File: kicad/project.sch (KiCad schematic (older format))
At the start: 23 parts, among them J1 SWD, U1 STM32L031F4Px

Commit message: Libraries
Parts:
- J1: symbol CONN_01X05 -> Conn_01x05
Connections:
- wire segments 12 -> 9
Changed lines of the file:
@@
 EESchema Schematic File Version 2
+LIBS:project-rescue
 LIBS:power
 LIBS:device
@@
 LIBS:valves
 LIBS:stm32_theapi
-LIBS:project-cache
 EELAYER 25 0
 EELAYER END
@@
 $EndComp
 $Comp
-L CONN_01X05 J1
+L Conn_01x05 J1
 U 1 1 5A9FF0BA
 P 2825 3625
@@
 	3025 3625 3525 3625
 Wire Wire Line
-	5575 2325 5575 2525
-Wire Wire Line
-	5575 2525 5575 2925
-Wire Wire Line
-	5675 2325 5675 2525
-Wire Wire Line
-	5675 2525 5675 2925
-Wire Wire Line
-	5575 2325 5625 2325
-Wire Wire Line
-	5625 2325 5675 2325
+	5575 2325 5575 2925
+Wire Wire Line
+	5675 2325 5675 2925
+Wire Wire Line
+	5575 2325 5675 2325
 Connection ~ 5625 2325
 Connection ~ 5675 2525

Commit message: Initial led placement
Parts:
- BT1: footprint Pin_Headers:Pin_Header_Straight_2x01_Pitch2.54mm -> theapi:CR2032H
- D1, D2, D3, D4, D5, D6, D7, D8: footprint (none) -> LEDs:LED_0805
- R2, R3, R4, R5, R6, R7, R8, R9: footprint (none) -> Resistors_SMD:R_0603_HandSoldering
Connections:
- net at U1.10 (PA4): now also R6.2
- net at U1.11 (PA5): now also R7.2
- net at U1.12 (PA6): now also R8.2
- net at U1.13 (PA7): now also R9.2
- net at U1.6 (PA0): now also R2.2
- net at U1.7 (PA1): now also R3.2
- net at U1.8 (PA2): now also R4.2
- net at U1.9 (PA3): now also R5.2
- no-connect marks 0 -> 5
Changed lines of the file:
@@
 LIBS:valves
 LIBS:stm32_theapi
+LIBS:project-cache
 EELAYER 25 0
 EELAYER END
@@
 $EndComp
 $Comp
-L GND #PWR13
+L GND #PWR01
 U 1 1 5A9FF0BC
 P 4950 3925
-F 0 "#PWR13" H 4950 3675 50  0001 C CNN
+F 0 "#PWR01" H 4950 3675 50  0001 C CNN
 F 1 "GND" H 4950 3775 50  0000 C CNN
 F 2 "" H 4950 3925 50  0001 C CNN
@@
 $EndComp
 $Comp
-L GND #PWR16
+L GND #PWR02
 U 1 1 5A9FF0BD
 P 5675 4825
-F 0 "#PWR16" H 5675 4575 50  0001 C CNN
+F 0 "#PWR02" H 5675 4575 50  0001 C CNN
 F 1 "GND" H 5675 4675 50  0000 C CNN
 F 2 "" H 5675 4825 50  0001 C CNN
@@
 SWDIO
 $Comp
-L +BATT #PWR4
+L +BATT #PWR03
 U 1 1 5A9FF0BE
 P 5625 2325
-F 0 "#PWR4" H 5625 2175 50  0001 C CNN
+F 0 "#PWR03" H 5625 2175 50  0001 C CNN
 F 1 "+BATT" H 5625 2465 50  0000 C CNN
 F 2 "" H 5625 2325 50  0001 C CNN
@@
 $EndComp
 $Comp
-L +BATT #PWR10
+L +BATT #PWR04
 U 1 1 5A9FF0BF
 P 3025 3425
-F 0 "#PWR10" H 3025 3275 50  0001 C CNN
+F 0 "#PWR04" H 3025 3275 50  0001 C CNN
 F 1 "+BATT" H 3025 3565 50  0000 C CNN
 F 2 "" H 3025 3425 50  0001 C CNN
@@
 $EndComp
 $Comp
-L GND #PWR11
+L GND #PWR05
 U 1 1 5A9FF0C0
 P 3525 3625
-F 0 "#PWR11" H 3525 3375 50  0001 C CNN
+F 0 "#PWR05" H 3525 3375 50  0001 C CNN
 F 1 "GND" H 3525 3475 50  0000 C CNN
 F 2 "" H 3525 3625 50  0001 C CNN
@@
 F 0 "BT1" H 4150 1675 50  0000 L CNN
 F 1 "Battery_Cell" H 4150 1575 50  0000 L CNN
-F 2 "Pin_Headers:Pin_Header_Straight_2x01_Pitch2.54mm" V 4050 1635 50  0001 C CNN
+F 2 "theapi:CR2032H" V 4050 1635 50  0001 C CNN
 F 3 "" V 4050 1635 50  0001 C CNN
 	1    4050 1575
@@
 $EndComp
 $Comp
-L +BATT #PWR1
+L +BATT #PWR06
 U 1 1 5A9FF0C2
 P 4050 1375
-F 0 "#PWR1" H 4050 1225 50  0001 C CNN
+F 0 "#PWR06" H 4050 1225 50  0001 C CNN
 F 1 "+BATT" H 4050 1515 50  0000 C CNN
 F 2 "" H 4050 1375 50  0001 C CNN
@@
 $EndComp
 $Comp
-L GND #PWR2
+L GND #PWR07
 U 1 1 5A9FF0C3
 P 4050 1675
-F 0 "#PWR2" H 4050 1425 50  0001 C CNN
+F 0 "#PWR07" H 4050 1425 50  0001 C CNN
 F 1 "GND" H 4050 1525 50  0000 C CNN
 F 2 "" H 4050 1675 50  0001 C CNN
@@
 $EndComp
 $Comp
-L GND #PWR5
+L GND #PWR08
 U 1 1 5A9FF0C6
 P 5375 2525
-F 0 "#PWR5" H 5375 2275 50  0001 C CNN
+F 0 "#PWR08" H 5375 2275 50  0001 C CNN
 F 1 "GND" H 5375 2375 50  0000 C CNN
 F 2 "" H 5375 2525 50  0001 C CNN
@@
 $EndComp
 $Comp
-L GND #PWR6
+L GND #PWR09
 U 1 1 5A9FF0C7
 P 5875 2525
-F 0 "#PWR6" H 5875 2275 50  0001 C CNN
+F 0 "#PWR09" H 5875 2275 50  0001 C CNN
 F 1 "GND" H 5875 2375 50  0000 C CNN
 F 2 "" H 5875 2525 50  0001 C CNN
@@
 F 0 "D1" H 9025 2275 50  0000 C CNN
 F 1 "LED" H 9025 2075 50  0000 C CNN
-F 2 "" H 9025 2175 50  0001 C CNN
+F 2 "LEDs:LED_0805" H 9025 2175 50  0001 C CNN
 F 3 "" H 9025 2175 50  0001 C CNN
 	1    9025 2175
@@
 $EndComp
 $Comp
-L GND #PWR3
+L GND #PWR010
 U 1 1 5A9FF286
 P 9175 2175
-F 0 "#PWR3" H 9175 1925 50  0001 C CNN
+F 0 "#PWR010" H 9175 1925 50  0001 C CNN
 F 1 "GND" H 9175 2025 50  0000 C CNN
 F 2 "" H 9175 2175 50  0001 C CNN
@@
 F 0 "R2" V 8805 2175 50  0000 C CNN
 F 1 "1k" V 8725 2175 50  0000 C CNN
-F 2 "" V 8655 2175 50  0001 C CNN
+F 2 "Resistors_SMD:R_0603_HandSoldering" V 8655 2175 50  0001 C CNN
 F 3 "" H 8725 2175 50  0001 C CNN
 	1    8725 2175
@@
 F 0 "D2" H 9025 2650 50  0000 C CNN
 F 1 "LED" H 9025 2450 50  0000 C CNN
-F 2 "" H 9025 2550 50  0001 C CNN
+F 2 "LEDs:LED_0805" H 9025 2550 50  0001 C CNN
 F 3 "" H 9025 2550 50  0001 C CNN
 	1    9025 2550
@@
 $EndComp
 $Comp
-L GND #PWR7
+L GND #PWR011
 U 1 1 5A9FF752
 P 9175 2550
-F 0 "#PWR7" H 9175 2300 50  0001 C CNN
+F 0 "#PWR011" H 9175 2300 50  0001 C CNN
 F 1 "GND" H 9175 2400 50  0000 C CNN
 F 2 "" H 9175 2550 50  0001 C CNN
@@
 F 0 "R3" V 8805 2550 50  0000 C CNN
 F 1 "1k" V 8725 2550 50  0000 C CNN
-F 2 "" V 8655 2550 50  0001 C CNN
+F 2 "Resistors_SMD:R_0603_HandSoldering" V 8655 2550 50  0001 C CNN
 F 3 "" H 8725 2550 50  0001 C CNN
 	1    8725 2550
@@
 F 0 "D3" H 9025 3050 50  0000 C CNN
 F 1 "LED" H 9025 2850 50  0000 C CNN
-F 2 "" H 9025 2950 50  0001 C CNN
+F 2 "LEDs:LED_0805" H 9025 2950 50  0001 C CNN
 F 3 "" H 9025 2950 50  0001 C CNN
 	1    9025 2950
@@
 $EndComp
 $Comp
-L GND #PWR8
+L GND #PWR012
 U 1 1 5A9FF7FA
 P 9175 2950
-F 0 "#PWR8" H 9175 2700 50  0001 C CNN
+F 0 "#PWR012" H 9175 2700 50  0001 C CNN
 F 1 "GND" H 9175 2800 50  0000 C CNN
 F 2 "" H 9175 2950 50  0001 C CNN
@@
 F 0 "R4" V 8805 2950 50  0000 C CNN
 F 1 "1k" V 8725 2950 50  0000 C CNN
-F 2 "" V 8655 2950 50  0001 C CNN
+F 2 "Resistors_SMD:R_0603_HandSoldering" V 8655 2950 50  0001 C CNN
 F 3 "" H 8725 2950 50  0001 C CNN
 	1    8725 2950
@@
 F 0 "D4" H 9025 3425 50  0000 C CNN
 F 1 "LED" H 9025 3225 50  0000 C CNN
-F 2 "" H 9025 3325 50  0001 C CNN
+F 2 "LEDs:LED_0805" H 9025 3325 50  0001 C CNN
 F 3 "" H 9025 3325 50  0001 C CNN
 	1    9025 3325
@@
 $EndComp
 $Comp
-L GND #PWR9
+L GND #PWR013
 U 1 1 5A9FF80C
 P 9175 3325
-F 0 "#PWR9" H 9175 3075 50  0001 C CNN
+F 0 "#PWR013" H 9175 3075 50  0001 C CNN
 F 1 "GND" H 9175 3175 50  0000 C CNN
 F 2 "" H 9175 3325 50  0001 C CNN
@@
 F 0 "R5" V 8805 3325 50  0000 C CNN
 F 1 "1k" V 8725 3325 50  0000 C CNN
-F 2 "" V 8655 3325 50  0001 C CNN
+F 2 "Resistors_SMD:R_0603_HandSoldering" V 8655 3325 50  0001 C CNN
 F 3 "" H 8725 3325 50  0001 C CNN
 	1    8725 3325
@@
 F 0 "D5" H 9025 3800 50  0000 C CNN
 F 1 "LED" H 9025 3600 50  0000 C CNN
-F 2 "" H 9025 3700 50  0001 C CNN
+F 2 "LEDs:LED_0805" H 9025 3700 50  0001 C CNN
 F 3 "" H 9025 3700 50  0001 C CNN
 	1    9025 3700
@@
 $EndComp
 $Comp
-L GND #PWR12
+L GND #PWR014
 U 1 1 5A9FFBFF
 P 9175 3700
-F 0 "#PWR12" H 9175 3450 50  0001 C CNN
+F 0 "#PWR014" H 9175 3450 50  0001 C CNN
 F 1 "GND" H 9175 3550 50  0000 C CNN
 F 2 "" H 9175 3700 50  0001 C CNN
@@
 F 0 "R6" V 8805 3700 50  0000 C CNN
 F 1 "1k" V 8725 3700 50  0000 C CNN
-F 2 "" V 8655 3700 50  0001 C CNN
+F 2 "Resistors_SMD:R_0603_HandSoldering" V 8655 3700 50  0001 C CNN
 F 3 "" H 8725 3700 50  0001 C CNN
 	1    8725 3700
@@
 F 0 "D6" H 9025 4175 50  0000 C CNN
 F 1 "LED" H 9025 3975 50  0000 C CNN
-F 2 "" H 9025 4075 50  0001 C CNN
+F 2 "LEDs:LED_0805" H 9025 4075 50  0001 C CNN
 F 3 "" H 9025 4075 50  0001 C CNN
 	1    9025 4075
@@
 $EndComp
 $Comp
-L GND #PWR14
+L GND #PWR015
 U 1 1 5A9FFC11
 P 9175 4075
-F 0 "#PWR14" H 9175 3825 50  0001 C CNN
+F 0 "#PWR015" H 9175 3825 50  0001 C CNN
 F 1 "GND" H 9175 3925 50  0000 C CNN
 F 2 "" H 9175 4075 50  0001 C CNN
@@
 F 0 "R7" V 8805 4075 50  0000 C CNN
 F 1 "1k" V 8725 4075 50  0000 C CNN
-F 2 "" V 8655 4075 50  0001 C CNN
+F 2 "Resistors_SMD:R_0603_HandSoldering" V 8655 4075 50  0001 C CNN
 F 3 "" H 8725 4075 50  0001 C CNN
 	1    8725 4075
@@
 F 0 "D7" H 9025 4575 50  0000 C CNN
 F 1 "LED" H 9025 4375 50  0000 C CNN
-F 2 "" H 9025 4475 50  0001 C CNN
+F 2 "LEDs:LED_0805" H 9025 4475 50  0001 C CNN
 F 3 "" H 9025 4475 50  0001 C CNN
 	1    9025 4475
@@
 $EndComp
 $Comp
-L GND #PWR15
+L GND #PWR016
 U 1 1 5A9FFC23
 P 9175 4475
-F 0 "#PWR15" H 9175 4225 50  0001 C CNN
+F 0 "#PWR016" H 9175 4225 50  0001 C CNN
 F 1 "GND" H 9175 4325 50  0000 C CNN
 F 2 "" H 9175 4475 50  0001 C CNN
@@
 F 0 "R8" V 8805 4475 50  0000 C CNN
 F 1 "1k" V 8725 4475 50  0000 C CNN
-F 2 "" V 8655 4475 50  0001 C CNN
+F 2 "Resistors_SMD:R_0603_HandSoldering" V 8655 4475 50  0001 C CNN
 F 3 "" H 8725 4475 50  0001 C CNN
 	1    8725 4475
@@
 F 0 "D8" H 9025 4950 50  0000 C CNN
 F 1 "LED" H 9025 4750 50  0000 C CNN
-F 2 "" H 9025 4850 50  0001 C CNN
+F 2 "LEDs:LED_0805" H 9025 4850 50  0001 C CNN
 F 3 "" H 9025 4850 50  0001 C CNN
 	1    9025 4850
@@
 $EndComp
 $Comp
-L GND #PWR17
+L GND #PWR017
 U 1 1 5A9FFC35
 P 9175 4850
-F 0 "#PWR17" H 9175 4600 50  0001 C CNN
+F 0 "#PWR017" H 9175 4600 50  0001 C CNN
 F 1 "GND" H 9175 4700 50  0000 C CNN
 F 2 "" H 9175 4850 50  0001 C CNN
@@
 F 0 "R9" V 8805 4850 50  0000 C CNN
 F 1 "1k" V 8725 4850 50  0000 C CNN
-F 2 "" V 8655 4850 50  0001 C CNN
+F 2 "Resistors_SMD:R_0603_HandSoldering" V 8655 4850 50  0001 C CNN
 F 3 "" H 8725 4850 50  0001 C CNN
 	1    8725 4850
 	0    1    1    0
 $EndComp
+Wire Wire Line
+	6175 3425 6650 3425
+Wire Wire Line
+	6650 3425 6650 2175
+Wire Wire Line
+	6650 2175 8575 2175
+Wire Wire Line
+	6175 3525 6750 3525
+Wire Wire Line
+	6750 3525 6750 2550
+Wire Wire Line
+	6750 2550 8575 2550
+Wire Wire Line
+	6175 3625 6850 3625
+Wire Wire Line
+	6850 3625 6850 2950
+Wire Wire Line
+	6850 2950 8575 2950
+Wire Wire Line
+	6175 3725 6975 3725
+Wire Wire Line
+	6975 3725 6975 3325
+Wire Wire Line
+	6975 3325 8575 3325
+Wire Wire Line
+	6175 3825 7100 3825
+Wire Wire Line
+	7100 3825 7100 3700
+Wire Wire Line
+	7100 3700 8575 3700
+Wire Wire Line
+	6175 3925 8425 3925
+Wire Wire Line
+	8425 3925 8425 4075
+Wire Wire Line
+	8425 4075 8575 4075
+Wire Wire Line
+	6175 4025 8300 4025
+Wire Wire Line
+	8300 4025 8300 4475
+Wire Wire Line
+	8300 4475 8575 4475
+Wire Wire Line
+	6175 4125 8175 4125
+Wire Wire Line
+	8175 4125 8175 4850
+Wire Wire Line
+	8175 4850 8575 4850
+NoConn ~ 6175 4225
+NoConn ~ 6175 4325
+NoConn ~ 5175 4225
+NoConn ~ 5175 4325
+NoConn ~ 5175 4525
 $EndSCHEMATC

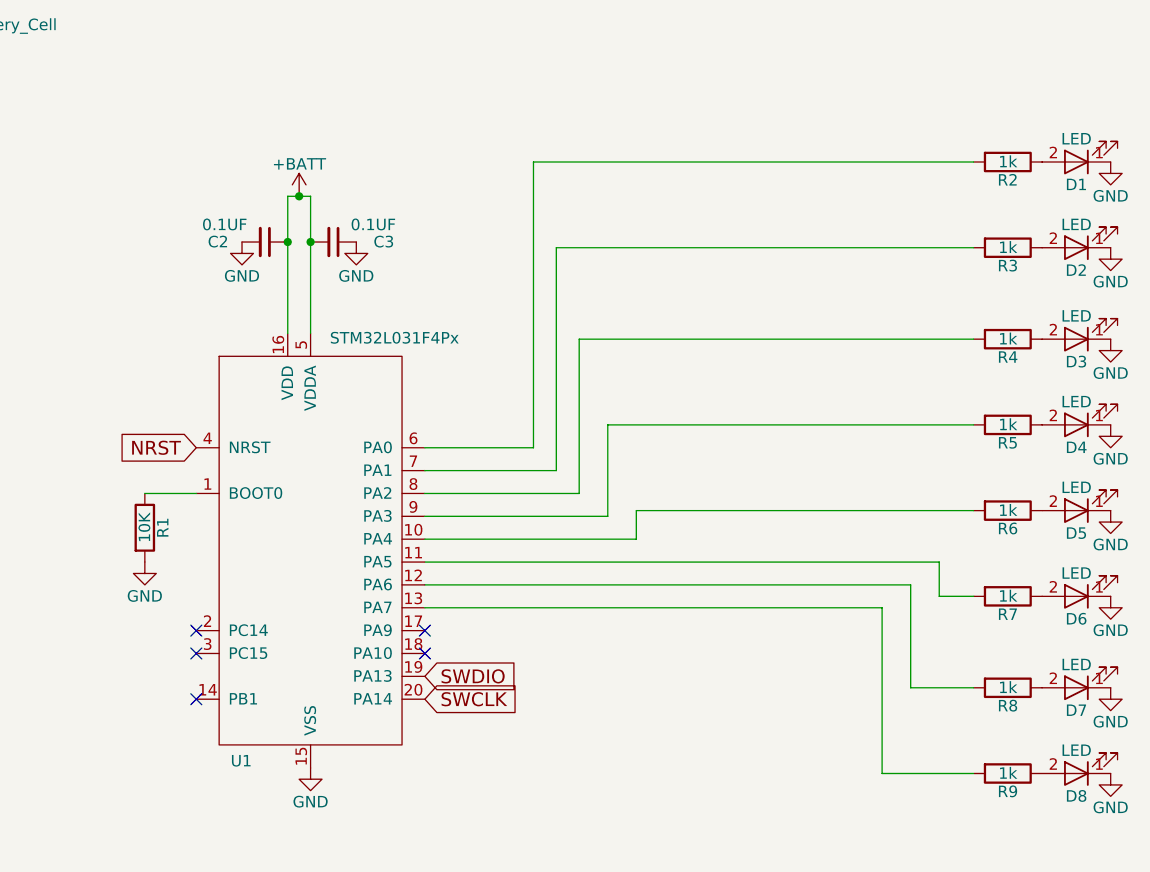
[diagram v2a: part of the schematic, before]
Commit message: 7 leds on individual pwm
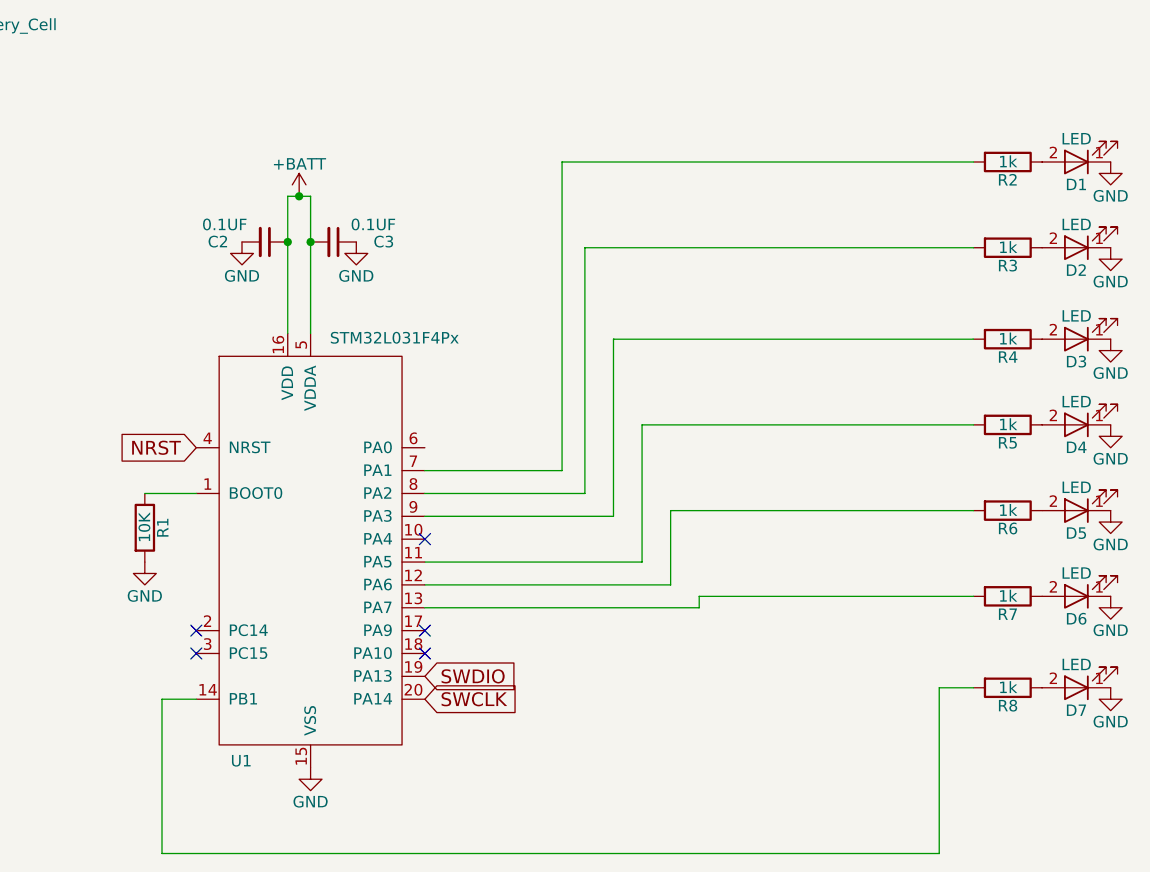
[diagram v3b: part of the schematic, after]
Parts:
- removed D8: LED, LEDs:LED_0805, symbol LED
- removed R9: 1k, Resistors_SMD:R_0603_HandSoldering, symbol R
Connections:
- net at U1.10 (PA4): no longer R6.2
- net at U1.11 (PA5): now also R5.2; no longer R7.2
- net at U1.12 (PA6): now also R6.2; no longer R8.2
- net at U1.13 (PA7): now also R7.2
- net at U1.14 (PB1): now also R8.2
- net at U1.6 (PA0): no longer R2.2
- net at U1.7 (PA1): now also R2.2; no longer R3.2
- net at U1.8 (PA2): now also R3.2; no longer R4.2
- net at U1.9 (PA3): now also R4.2; no longer R5.2
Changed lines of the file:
@@
 $EndComp
 $Comp
-L GND #PWR01
+L GND #PWR5
 U 1 1 5A9FF0BC
 P 4950 3925
-F 0 "#PWR01" H 4950 3675 50  0001 C CNN
+F 0 "#PWR5" H 4950 3675 50  0001 C CNN
 F 1 "GND" H 4950 3775 50  0000 C CNN
 F 2 "" H 4950 3925 50  0001 C CNN
@@
 $EndComp
 $Comp
-L GND #PWR02
+L GND #PWR8
 U 1 1 5A9FF0BD
 P 5675 4825
-F 0 "#PWR02" H 5675 4575 50  0001 C CNN
+F 0 "#PWR8" H 5675 4575 50  0001 C CNN
 F 1 "GND" H 5675 4675 50  0000 C CNN
 F 2 "" H 5675 4825 50  0001 C CNN
@@
 SWDIO
 $Comp
-L +BATT #PWR03
+L +BATT #PWR7
 U 1 1 5A9FF0BE
 P 5625 2325
-F 0 "#PWR03" H 5625 2175 50  0001 C CNN
+F 0 "#PWR7" H 5625 2175 50  0001 C CNN
 F 1 "+BATT" H 5625 2465 50  0000 C CNN
 F 2 "" H 5625 2325 50  0001 C CNN
@@
 $EndComp
 $Comp
-L +BATT #PWR04
+L +BATT #PWR1
 U 1 1 5A9FF0BF
 P 3025 3425
-F 0 "#PWR04" H 3025 3275 50  0001 C CNN
+F 0 "#PWR1" H 3025 3275 50  0001 C CNN
 F 1 "+BATT" H 3025 3565 50  0000 C CNN
 F 2 "" H 3025 3425 50  0001 C CNN
@@
 $EndComp
 $Comp
-L GND #PWR05
+L GND #PWR2
 U 1 1 5A9FF0C0
 P 3525 3625
-F 0 "#PWR05" H 3525 3375 50  0001 C CNN
+F 0 "#PWR2" H 3525 3375 50  0001 C CNN
 F 1 "GND" H 3525 3475 50  0000 C CNN
 F 2 "" H 3525 3625 50  0001 C CNN
@@
 $EndComp
 $Comp
-L +BATT #PWR06
+L +BATT #PWR3
 U 1 1 5A9FF0C2
 P 4050 1375
-F 0 "#PWR06" H 4050 1225 50  0001 C CNN
+F 0 "#PWR3" H 4050 1225 50  0001 C CNN
 F 1 "+BATT" H 4050 1515 50  0000 C CNN
 F 2 "" H 4050 1375 50  0001 C CNN
@@
 $EndComp
 $Comp
-L GND #PWR07
+L GND #PWR4
 U 1 1 5A9FF0C3
 P 4050 1675
-F 0 "#PWR07" H 4050 1425 50  0001 C CNN
+F 0 "#PWR4" H 4050 1425 50  0001 C CNN
 F 1 "GND" H 4050 1525 50  0000 C CNN
 F 2 "" H 4050 1675 50  0001 C CNN
@@
 $EndComp
 $Comp
-L GND #PWR08
+L GND #PWR6
 U 1 1 5A9FF0C6
 P 5375 2525
-F 0 "#PWR08" H 5375 2275 50  0001 C CNN
+F 0 "#PWR6" H 5375 2275 50  0001 C CNN
 F 1 "GND" H 5375 2375 50  0000 C CNN
 F 2 "" H 5375 2525 50  0001 C CNN
@@
 $EndComp
 $Comp
-L GND #PWR09
+L GND #PWR9
 U 1 1 5A9FF0C7
 P 5875 2525
-F 0 "#PWR09" H 5875 2275 50  0001 C CNN
+F 0 "#PWR9" H 5875 2275 50  0001 C CNN
 F 1 "GND" H 5875 2375 50  0000 C CNN
 F 2 "" H 5875 2525 50  0001 C CNN
@@
 $EndComp
 $Comp
-L GND #PWR010
+L GND #PWR10
 U 1 1 5A9FF286
 P 9175 2175
-F 0 "#PWR010" H 9175 1925 50  0001 C CNN
+F 0 "#PWR10" H 9175 1925 50  0001 C CNN
 F 1 "GND" H 9175 2025 50  0000 C CNN
 F 2 "" H 9175 2175 50  0001 C CNN
@@
 $EndComp
 $Comp
-L GND #PWR011
+L GND #PWR11
 U 1 1 5A9FF752
 P 9175 2550
-F 0 "#PWR011" H 9175 2300 50  0001 C CNN
+F 0 "#PWR11" H 9175 2300 50  0001 C CNN
 F 1 "GND" H 9175 2400 50  0000 C CNN
 F 2 "" H 9175 2550 50  0001 C CNN
@@
 $EndComp
 $Comp
-L GND #PWR012
+L GND #PWR12
 U 1 1 5A9FF7FA
 P 9175 2950
-F 0 "#PWR012" H 9175 2700 50  0001 C CNN
+F 0 "#PWR12" H 9175 2700 50  0001 C CNN
 F 1 "GND" H 9175 2800 50  0000 C CNN
 F 2 "" H 9175 2950 50  0001 C CNN
@@
 $EndComp
 $Comp
-L GND #PWR013
+L GND #PWR13
 U 1 1 5A9FF80C
 P 9175 3325
-F 0 "#PWR013" H 9175 3075 50  0001 C CNN
+F 0 "#PWR13" H 9175 3075 50  0001 C CNN
 F 1 "GND" H 9175 3175 50  0000 C CNN
 F 2 "" H 9175 3325 50  0001 C CNN
@@
 $EndComp
 $Comp
-L GND #PWR014
+L GND #PWR14
 U 1 1 5A9FFBFF
 P 9175 3700
-F 0 "#PWR014" H 9175 3450 50  0001 C CNN
+F 0 "#PWR14" H 9175 3450 50  0001 C CNN
 F 1 "GND" H 9175 3550 50  0000 C CNN
 F 2 "" H 9175 3700 50  0001 C CNN
@@
 $EndComp
 $Comp
-L GND #PWR015
+L GND #PWR15
 U 1 1 5A9FFC11
 P 9175 4075
-F 0 "#PWR015" H 9175 3825 50  0001 C CNN
+F 0 "#PWR15" H 9175 3825 50  0001 C CNN
 F 1 "GND" H 9175 3925 50  0000 C CNN
 F 2 "" H 9175 4075 50  0001 C CNN
@@
 $EndComp
 $Comp
-L GND #PWR016
+L GND #PWR16
 U 1 1 5A9FFC23
 P 9175 4475
-F 0 "#PWR016" H 9175 4225 50  0001 C CNN
+F 0 "#PWR16" H 9175 4225 50  0001 C CNN
 F 1 "GND" H 9175 4325 50  0000 C CNN
 F 2 "" H 9175 4475 50  0001 C CNN
@@
 	0    1    1    0
 $EndComp
-$Comp
-L LED D8
-U 1 1 5A9FFC2F
-P 9025 4850
-F 0 "D8" H 9025 4950 50  0000 C CNN
-F 1 "LED" H 9025 4750 50  0000 C CNN
-F 2 "LEDs:LED_0805" H 9025 4850 50  0001 C CNN
-F 3 "" H 9025 4850 50  0001 C CNN
-	1    9025 4850
-	-1   0    0    1
-$EndComp
-$Comp
-L GND #PWR017
-U 1 1 5A9FFC35
-P 9175 4850
-F 0 "#PWR017" H 9175 4600 50  0001 C CNN
-F 1 "GND" H 9175 4700 50  0000 C CNN
-F 2 "" H 9175 4850 50  0001 C CNN
-F 3 "" H 9175 4850 50  0001 C CNN
-	1    9175 4850
-	1    0    0    -1
-$EndComp
-$Comp
-L R R9
-U 1 1 5A9FFC3B
-P 8725 4850
-F 0 "R9" V 8805 4850 50  0000 C CNN
-F 1 "1k" V 8725 4850 50  0000 C CNN
-F 2 "Resistors_SMD:R_0603_HandSoldering" V 8655 4850 50  0001 C CNN
-F 3 "" H 8725 4850 50  0001 C CNN
-	1    8725 4850
-	0    1    1    0
-$EndComp
-Wire Wire Line
-	6175 3425 6650 3425
-Wire Wire Line
-	6650 3425 6650 2175
-Wire Wire Line
-	6650 2175 8575 2175
-Wire Wire Line
-	6175 3525 6750 3525
-Wire Wire Line
-	6750 3525 6750 2550
-Wire Wire Line
-	6750 2550 8575 2550
-Wire Wire Line
-	6175 3625 6850 3625
-Wire Wire Line
-	6850 3625 6850 2950
-Wire Wire Line
-	6850 2950 8575 2950
-Wire Wire Line
-	6175 3725 6975 3725
-Wire Wire Line
-	6975 3725 6975 3325
-Wire Wire Line
-	6975 3325 8575 3325
-Wire Wire Line
-	6175 3825 7100 3825
-Wire Wire Line
-	7100 3825 7100 3700
-Wire Wire Line
-	7100 3700 8575 3700
-Wire Wire Line
-	6175 3925 8425 3925
-Wire Wire Line
-	8425 3925 8425 4075
-Wire Wire Line
-	8425 4075 8575 4075
-Wire Wire Line
-	6175 4025 8300 4025
-Wire Wire Line
-	8300 4025 8300 4475
-Wire Wire Line
-	8300 4475 8575 4475
-Wire Wire Line
-	6175 4125 8175 4125
-Wire Wire Line
-	8175 4125 8175 4850
-Wire Wire Line
-	8175 4850 8575 4850
 NoConn ~ 6175 4225
 NoConn ~ 6175 4325
 NoConn ~ 5175 4225
 NoConn ~ 5175 4325
-NoConn ~ 5175 4525
+Wire Wire Line
+	6175 3525 6775 3525
+Wire Wire Line
+	6775 3525 6775 2175
+Wire Wire Line
+	6775 2175 8575 2175
+Wire Wire Line
+	6175 3625 6875 3625
+Wire Wire Line
+	6875 3625 6875 2550
+Wire Wire Line
+	6875 2550 8575 2550
+Wire Wire Line
+	6175 3725 7000 3725
+Wire Wire Line
+	7000 3725 7000 2950
+Wire Wire Line
+	7000 2950 8575 2950
+Wire Wire Line
+	6175 3925 7125 3925
+Wire Wire Line
+	7125 3925 7125 3325
+Wire Wire Line
+	7125 3325 8575 3325
+Wire Wire Line
+	6175 4025 7250 4025
+Wire Wire Line
+	7250 4025 7250 3700
+Wire Wire Line
+	7250 3700 8575 3700
+Wire Wire Line
+	6175 4125 7375 4125
+Wire Wire Line
+	7375 4125 7375 4075
+Wire Wire Line
+	7375 4075 8575 4075
+Wire Wire Line
+	5175 4525 5025 4525
+Wire Wire Line
+	5025 4525 5025 5200
+Wire Wire Line
+	5025 5200 8425 5200
+Wire Wire Line
+	8425 5200 8425 4475
+Wire Wire Line
+	8425 4475 8575 4475
+NoConn ~ 6175 3825
 $EndSCHEMATC
